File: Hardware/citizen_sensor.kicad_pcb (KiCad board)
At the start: 2 copper layers, 52 x 80 mm, 74 parts, among them J1 BATT, J2 USB_B_Micro, J3 VEML6075, J4 BME280, J5 PROG, J6 CSS811, J7 MAX30105, Q1 2N7002, SW1 RST, U1 TLC2272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

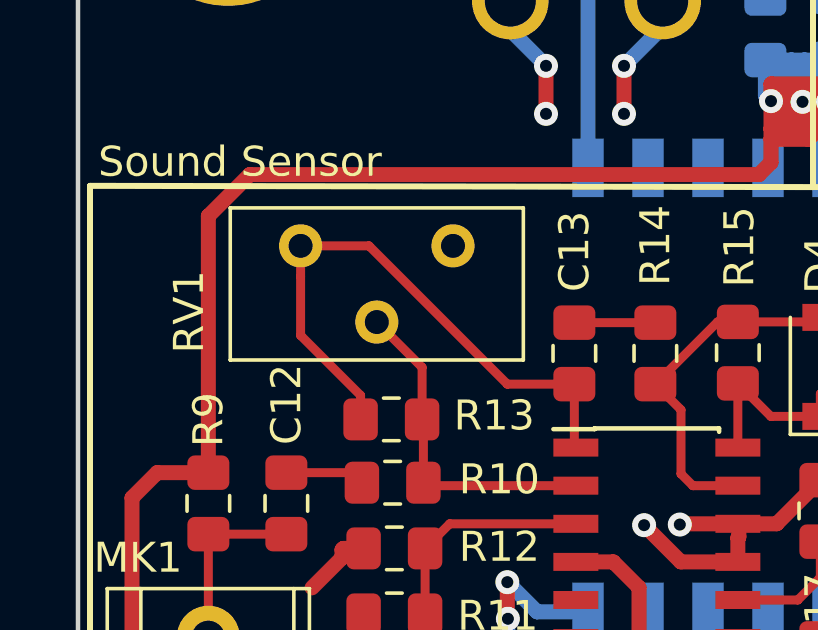
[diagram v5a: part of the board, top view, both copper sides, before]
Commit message: Update compnent placement and pot
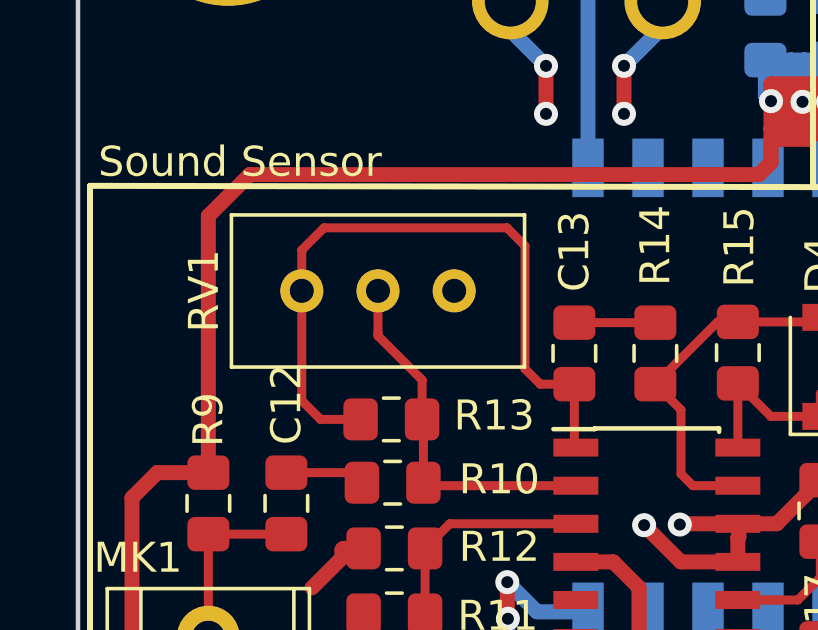
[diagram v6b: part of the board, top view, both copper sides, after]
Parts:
- RV1: footprint Potentiometer_THT:Potentiometer_Bourns_3386X_Horizontal -> Potentiometer_THT:Potentiometer_Bourns_3296W_Vertical
- moved RV1 1.50 mm to (136.5, 57.7), turned to 0 degrees
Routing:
- net Net-(C13-Pad1): track 19.8 -> 23.3 mm
- net Net-(R10-Pad1): track 11.1 -> 12.1 mm
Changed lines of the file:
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@@
-(kicad_pcb (version 20171130) (host pcbnew "(5.0.2)-1")
+(kicad_pcb (version 20171130) (host pcbnew "(5.0.1-3-g963ef8bb5)")
   (general
     (thickness 1.6)
     (drawings 49)
-    (tracks 748)
+    (tracks 753)
     (zones 0)
     (modules 74)
@@
   )
   (layers
-    (0 F.Cu signal)
-    (31 B.Cu signal)
+    (0 F.Cu signal hide)
+    (31 B.Cu signal hide)
     (32 B.Adhes user)
     (33 F.Adhes user)
@@
     (pad 1 thru_hole circle (at 0 0) (size 6.4 6.4) (drill 3.2) (layers *.Cu *.Mask))
   )
-  (module Potentiometer_THT:Potentiometer_Bourns_3386X_Horizontal (layer F.Cu)
-    (at 136.5 56.2 270)
-    (descr "Potentiometer, horizontal, Bourns 3386X, https://www.bourns.com/pdfs/3386.pdf")
-    (tags "Potentiometer horizontal Bourns 3386X")
-    (fp_text reference RV1 (at 2.2 8.8 270) (layer F.SilkS)
-      (effects (font (size 1 1) (thickness 0.15)))
-    )
-    (fp_text value "100K GAIN" (at 0 8.555 270) (layer F.Fab)
-      (effects (font (size 1 1) (thickness 0.15)))
-    )
-    (fp_text user %R (at 1.27 2.54 270) (layer F.Fab)
-      (effects (font (size 1 1) (thickness 0.15)))
-    )
-    (fp_line (start 3.94 -2.48) (end -1.4 -2.48) (layer F.CrtYd) (width 0.05))
-    (fp_line (start 3.94 7.56) (end 3.94 -2.48) (layer F.CrtYd) (width 0.05))
-    (fp_line (start -1.4 7.56) (end 3.94 7.56) (layer F.CrtYd) (width 0.05))
-    (fp_line (start -1.4 -2.48) (end -1.4 7.56) (layer F.CrtYd) (width 0.05))
-    (fp_line (start -1.265 -2.345) (end -1.265 7.425) (layer F.SilkS) (width 0.12))
-    (fp_line (start 3.805 -2.345) (end 3.805 7.425) (layer F.SilkS) (width 0.12))
-    (fp_line (start -1.265 7.425) (end 3.805 7.425) (layer F.SilkS) (width 0.12))
-    (fp_line (start -1.265 -2.345) (end 3.805 -2.345) (layer F.SilkS) (width 0.12))
-    (fp_line (start -1.145 -2.225) (end 3.685 -2.225) (layer F.Fab) (width 0.1))
-    (fp_line (start -1.145 7.305) (end -1.145 -2.225) (layer F.Fab) (width 0.1))
-    (fp_line (start 3.685 7.305) (end -1.145 7.305) (layer F.Fab) (width 0.1))
-    (fp_line (start 3.685 -2.225) (end 3.685 7.305) (layer F.Fab) (width 0.1))
-    (pad 1 thru_hole circle (at 0 0 270) (size 1.44 1.44) (drill 0.8) (layers *.Cu *.Mask)
-      (net 43 "Net-(RV1-Pad1)"))
-    (pad 2 thru_hole circle (at 2.54 2.54 270) (size 1.44 1.44) (drill 0.8) (layers *.Cu *.Mask)
-      (net 37 "Net-(R10-Pad1)"))
-    (pad 3 thru_hole circle (at 0 5.08 270) (size 1.44 1.44) (drill 0.8) (layers *.Cu *.Mask)
-      (net 10 "Net-(C13-Pad1)"))
-    (model ${KISYS3DMOD}/Potentiometer_THT.3dshapes/Potentiometer_Bourns_3386X_Horizontal.wrl
-      (at (xyz 0 0 0))
-      (scale (xyz 1 1 1))
-      (rotate (xyz 0 0 0))
-    )
-  )
   (module Aesthetics:electronic_cats_logo_8x6 (layer F.Cu)
     (at 161.65 74.2)
@@
       (xy -2.008909 -4.08709) (xy -2.00878 -4.3815)) (layer B.SilkS) (width 0.01))
   )
+  (module Potentiometer_THT:Potentiometer_Bourns_3296W_Vertical (layer F.Cu)
+    (at 136.54 57.7)
+    (descr "Potentiometer, vertical, Bourns 3296W, https://www.bourns.com/pdfs/3296.pdf")
+    (tags "Potentiometer vertical Bourns 3296W")
+    (fp_text reference RV1 (at -8.34 0 270) (layer F.SilkS)
+      (effects (font (size 1 1) (thickness 0.15)))
+    )
+    (fp_text value "100K GAIN" (at -2.54 3.67) (layer F.Fab)
+      (effects (font (size 1 1) (thickness 0.15)))
+    )
+    (fp_circle (center 0.955 1.15) (end 2.05 1.15) (layer F.Fab) (width 0.1))
+    (fp_line (start -7.305 -2.41) (end -7.305 2.42) (layer F.Fab) (width 0.1))
+    (fp_line (start -7.305 2.42) (end 2.225 2.42) (layer F.Fab) (width 0.1))
+    (fp_line (start 2.225 2.42) (end 2.225 -2.41) (layer F.Fab) (width 0.1))
+    (fp_line (start 2.225 -2.41) (end -7.305 -2.41) (layer F.Fab) (width 0.1))
+    (fp_line (start 0.955 2.235) (end 0.956 0.066) (layer F.Fab) (width 0.1))
+    (fp_line (start 0.955 2.235) (end 0.956 0.066) (layer F.Fab) (width 0.1))
+    (fp_line (start -7.425 -2.53) (end 2.345 -2.53) (layer F.SilkS) (width 0.12))
+    (fp_line (start -7.425 2.54) (end 2.345 2.54) (layer F.SilkS) (width 0.12))
+    (fp_line (start -7.425 -2.53) (end -7.425 2.54) (layer F.SilkS) (width 0.12))
+    (fp_line (start 2.345 -2.53) (end 2.345 2.54) (layer F.SilkS) (width 0.12))
+    (fp_line (start -7.6 -2.7) (end -7.6 2.7) (layer F.CrtYd) (width 0.05))
+    (fp_line (start -7.6 2.7) (end 2.5 2.7) (layer F.CrtYd) (width 0.05))
+    (fp_line (start 2.5 2.7) (end 2.5 -2.7) (layer F.CrtYd) (width 0.05))
+    (fp_line (start 2.5 -2.7) (end -7.6 -2.7) (layer F.CrtYd) (width 0.05))
+    (fp_text user %R (at -3.175 0.005) (layer F.Fab)
+      (effects (font (size 1 1) (thickness 0.15)))
+    )
+    (pad 1 thru_hole circle (at 0 0) (size 1.44 1.44) (drill 0.8) (layers *.Cu *.Mask)
+      (net 43 "Net-(RV1-Pad1)"))
+    (pad 2 thru_hole circle (at -2.54 0) (size 1.44 1.44) (drill 0.8) (layers *.Cu *.Mask)
+      (net 37 "Net-(R10-Pad1)"))
+    (pad 3 thru_hole circle (at -5.08 0) (size 1.44 1.44) (drill 0.8) (layers *.Cu *.Mask)
+      (net 10 "Net-(C13-Pad1)"))
+    (model ${KISYS3DMOD}/Potentiometer_THT.3dshapes/Potentiometer_Bourns_3296W_Vertical.wrl
+      (at (xyz 0 0 0))
+      (scale (xyz 1 1 1))
+      (rotate (xyz 0 0 0))
+    )
+  )
   (gr_text Charged (at 160.85 57.1) (layer F.SilkS)
     (effects (font (size 1 1) (thickness 0.2)))
@@
   (segment (start 130.945 63.76) (end 133.1276 63.76) (width 0.3) (layer F.Cu) (net 8))
   (segment (start 143.245 58.76) (end 140.545 58.76) (width 0.3) (layer F.Cu) (net 9))
-  (segment (start 131.42 57.218233) (end 131.42 56.2) (width 0.3) (layer F.Cu) (net 10))
-  (segment (start 131.42 59.185) (end 131.42 57.218233) (width 0.3) (layer F.Cu) (net 10))
-  (segment (start 133.42 61.185) (end 131.42 59.185) (width 0.3) (layer F.Cu) (net 10))
-  (segment (start 133.42 61.985) (end 133.42 61.185) (width 0.3) (layer F.Cu) (net 10))
-  (segment (start 140.545 60.81) (end 138.31 60.81) (width 0.3) (layer F.Cu) (net 10))
-  (segment (start 133.7 56.2) (end 131.42 56.2) (width 0.3) (layer F.Cu) (net 10))
-  (segment (start 138.31 60.81) (end 133.7 56.2) (width 0.3) (layer F.Cu) (net 10))
   (segment (start 140.545 62.875) (end 140.595 62.925) (width 0.3) (layer F.Cu) (net 10))
   (segment (start 140.545 60.81) (end 140.545 62.875) (width 0.3) (layer F.Cu) (net 10))
+  (segment (start 139.41 60.81) (end 140.545 60.81) (width 0.3) (layer F.Cu) (net 10))
+  (segment (start 138.9 56.2) (end 138.9 60.3) (width 0.3) (layer F.Cu) (net 10))
+  (segment (start 138.3 55.6) (end 138.9 56.2) (width 0.3) (layer F.Cu) (net 10))
+  (segment (start 138.9 60.3) (end 139.41 60.81) (width 0.3) (layer F.Cu) (net 10))
+  (segment (start 132.2 55.6) (end 138.3 55.6) (width 0.3) (layer F.Cu) (net 10))
+  (segment (start 131.46 56.34) (end 132.2 55.6) (width 0.3) (layer F.Cu) (net 10))
+  (segment (start 131.46 57.7) (end 131.46 56.34) (width 0.3) (layer F.Cu) (net 10))
+  (segment (start 133.42 61.985) (end 132.085 61.985) (width 0.3) (layer F.Cu) (net 10))
+  (segment (start 131.46 61.36) (end 131.46 57.7) (width 0.3) (layer F.Cu) (net 10))
+  (segment (start 132.085 61.985) (end 131.46 61.36) (width 0.3) (layer F.Cu) (net 10))
   (segment (start 145.995 68.005) (end 147.995 68.005) (width 0.3) (layer F.Cu) (net 11))
   (segment (start 148.745 67.255) (end 148.745 66.06) (width 0.3) (layer F.Cu) (net 11))
@@
   (segment (start 135.513 62.028) (end 135.47 61.985) (width 0.3) (layer F.Cu) (net 37))
   (segment (start 135.513 64.0954) (end 135.513 62.028) (width 0.3) (layer F.Cu) (net 37))
-  (segment (start 135.47 60.25) (end 133.96 58.74) (width 0.3) (layer F.Cu) (net 37))
-  (segment (start 135.47 61.985) (end 135.47 60.25) (width 0.3) (layer F.Cu) (net 37))
   (segment (start 135.6126 64.195) (end 135.513 64.0954) (width 0.3) (layer F.Cu) (net 37))
   (segment (start 140.595 64.195) (end 135.6126 64.195) (width 0.3) (layer F.Cu) (net 37))
+  (segment (start 135.47 61.985) (end 135.47 60.67) (width 0.3) (layer F.Cu) (net 37))
+  (segment (start 135.47 60.67) (end 134 59.2) (width 0.3) (layer F.Cu) (net 37))
+  (segment (start 134 59.2) (end 134 59.1) (width 0.3) (layer F.Cu) (net 37))
+  (segment (start 134 57.7) (end 134 59.1) (width 0.3) (layer F.Cu) (net 37))
   (segment (start 136.39 65.465) (end 140.595 65.465) (width 0.3) (layer F.Cu) (net 38))
   (segment (start 135.57 66.285) (end 136.39 65.465) (width 0.3) (layer F.Cu) (net 38))

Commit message: fabcity logo
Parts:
- added G***: LOGO, Aesthetics:fabcity, F.Cu at (161.8, 65.7)
- added G***: LOGO, Aesthetics:fabcity, B.Cu at (151.1, 104.5)
- moved G*** 9.23 mm to (130.8, 103.7)
- moved G*** 9.17 mm to (169.6, 104.0)
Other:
- board text removed: "CatWAN Citizen"
- board text removed: "V0.1"
- board text removed: "v0.1"
